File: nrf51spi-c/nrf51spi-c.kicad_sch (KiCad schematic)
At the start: 23 parts, among them J1 Conn_01x09, J2 Conn_01x07, U1 nRF51x22-QFxx, Y1 16MHz

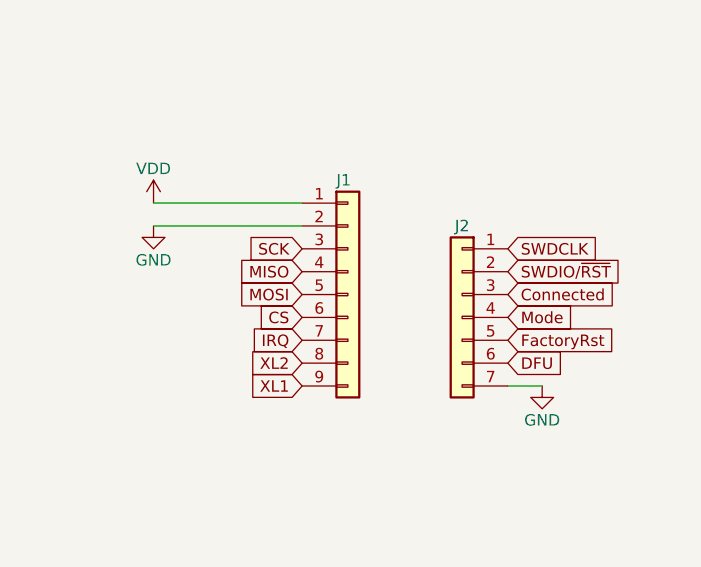
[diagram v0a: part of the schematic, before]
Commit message: Add teradrops and castellated holes
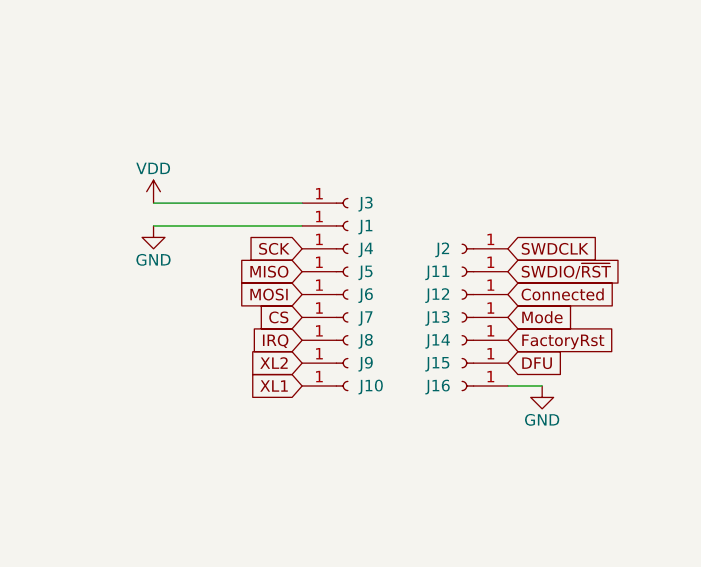
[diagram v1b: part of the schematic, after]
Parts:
- removed J1: Conn_01x09, Connector_PinHeader_1.27mm:PinHeader_1x09_P1.27mm_Vertical, symbol Connector_Generic:Conn_01x09
- removed J2: Conn_01x07, Connector_PinHeader_1.27mm:PinHeader_1x07_P1.27mm_Vertical, symbol Connector_Generic:Conn_01x07
- added J1, J10, J11, J12, J13, J14, J15, J16, J2, J3, J4, J5, J6, J7, J8, J9: Conn_01x01_Socket, nrf51_module:castellated_holes_1.27mm, symbol Connector:Conn_01x01_Socket
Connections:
- net CS: now also J7.1 (Pin_1)
- net Connected: now also J12.1 (Pin_1)
- net DFU: now also J15.1 (Pin_1)
- net FactoryRst: now also J14.1 (Pin_1)
- net GND: now also J1.1 (Pin_1), J16.1 (Pin_1)
- net IRQ: now also J8.1 (Pin_1)
- net MISO: now also J5.1 (Pin_1)
- net MOSI: now also J6.1 (Pin_1)
- net Mode: now also J13.1 (Pin_1)
- net SCK: now also J4.1 (Pin_1)
- net SWDCLK: now also J2.1 (Pin_1)
- net SWDIO/~{RST}: now also J11.1 (Pin_1)
- net VDD: now also J3.1 (Pin_1)
- net XL1: now also J10.1 (Pin_1)
- net XL2: now also J9.1 (Pin_1)
